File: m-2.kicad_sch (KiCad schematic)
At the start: 26 parts, among them J2 1-2199230-6, Y1 ECS-327MVATX-2-CN-TR3

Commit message: Layout cleanup, silk
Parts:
- TP10, TP11, TP12: footprint JetsonCarrier:TP_SMD_0.75mm -> TestPoint:TestPoint_Pad_D1.0mm
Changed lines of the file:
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@@
 			)
 		)
-		(property "Footprint" "JetsonCarrier:TP_SMD_0.75mm"
+		(property "Footprint" "TestPoint:TestPoint_Pad_D1.0mm"
 			(at 245.11 128.27 0)
 			(hide yes)
@@
 			)
 		)
-		(property "Footprint" "JetsonCarrier:TP_SMD_0.75mm"
+		(property "Footprint" "TestPoint:TestPoint_Pad_D1.0mm"
 			(at 245.11 130.81 0)
 			(hide yes)
@@
 			)
 		)
-		(property "Footprint" "JetsonCarrier:TP_SMD_0.75mm"
+		(property "Footprint" "TestPoint:TestPoint_Pad_D1.0mm"
 			(at 245.11 133.35 0)
 			(hide yes)

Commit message: route all diff pairs, length tuning
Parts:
- renumbered C25 to C10, C13 to C11, C14 to C12, C15 to C13, C16 to C14, C17 to C15, C18 to C16, C19 to C17, C20 to C18, C21 to C19, C22 to C20, C23 to C21, C24 to C22, D1 to D3, R13 to R16, R37 to R17, R38 to R18, R39 to R19, R19 to R20, R143 to R21, TP10 to TP3, TP11 to TP4, TP12 to TP5

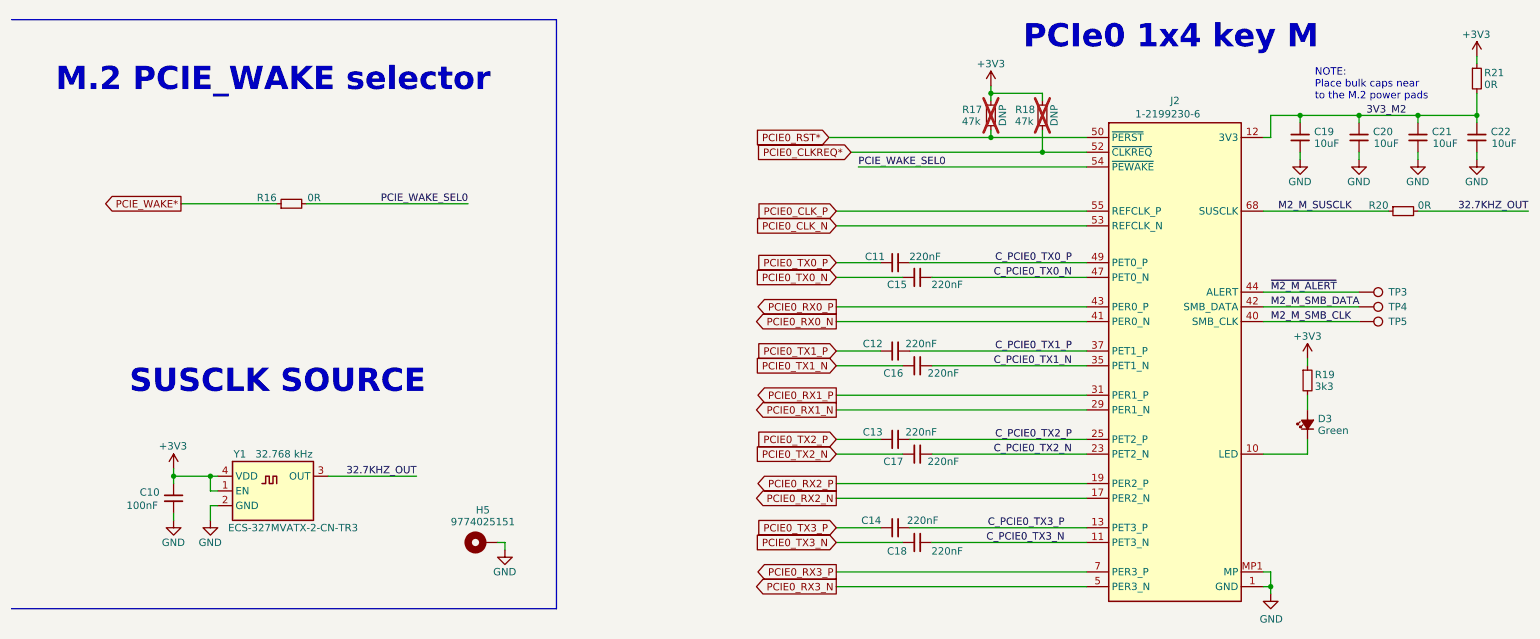
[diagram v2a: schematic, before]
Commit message: Replace current monitor w/ INA226 (addr = 0x42)
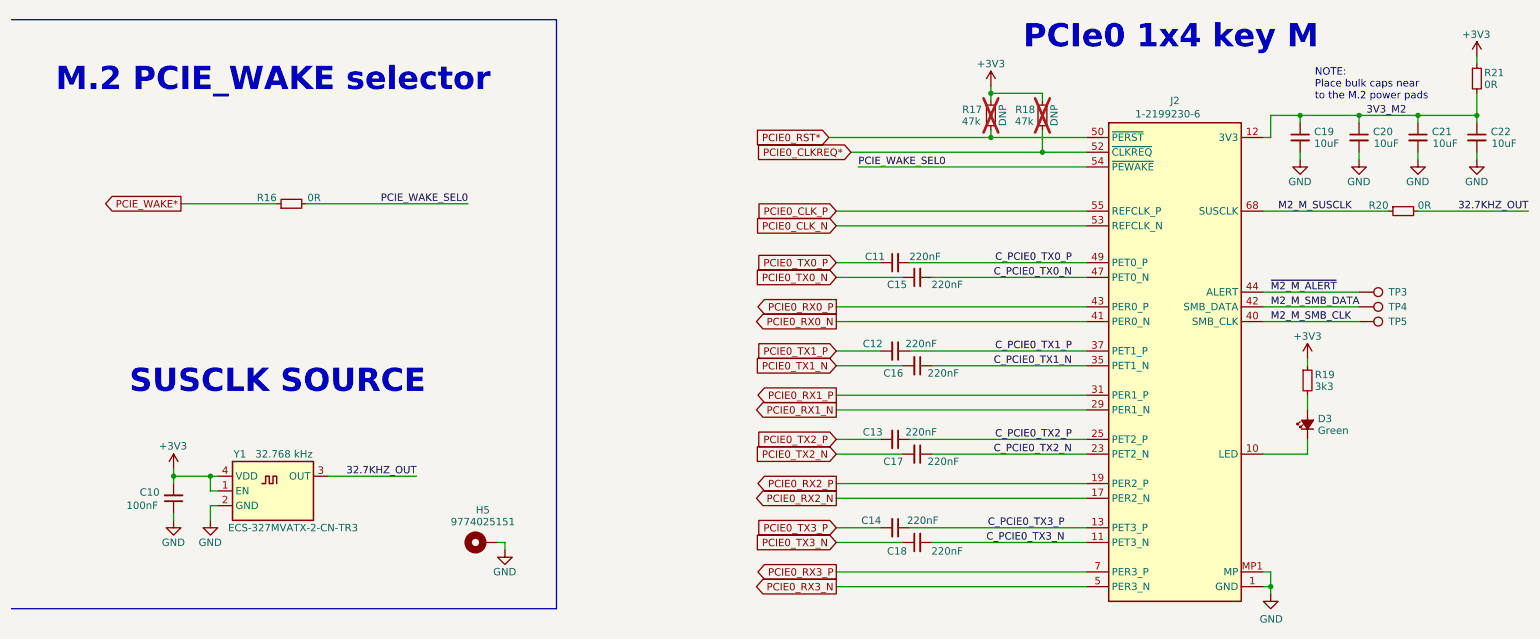
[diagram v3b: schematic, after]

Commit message: Final BOM changes, gerbers
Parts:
- C10: LCSC (none) -> C14663
- C11, C12, C13, C14, C15, C16, C17, C18: LCSC (none) -> C16772
- C19, C20, C21, C22: LCSC (none) -> C96446
- D3: LCSC (none) -> C12065
- J2: LCSC (none) -> C4710843
- R16, R20: LCSC (none) -> C17168
- R17, R18: LCSC (none) -> C25792
- R19: LCSC (none) -> C22978
- R21: LCSC (none) -> C21189
- Y1: LCSC (none) -> C5375606
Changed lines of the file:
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@@
 			)
 		)
+		(property "LCSC" "C5375606"
+			(at 52.07 151.13 0)
+			(effects
+				(font
+					(size 1.27 1.27)
+				)
+				(hide yes)
+			)
+		)
 		(pin "2"
 		)
@@
 			)
 		)
+		(property "LCSC" "C25792"
+			(at 189.23 92.456 0)
+			(effects
+				(font
+					(size 1.27 1.27)
+				)
+				(hide yes)
+			)
+		)
 		(pin "1"
 		)
@@
 			)
 		)
+		(property "LCSC" "C16772"
+			(at 159.512 132.842 0)
+			(effects
+				(font
+					(size 1.27 1.27)
+				)
+				(hide yes)
+			)
+		)
 		(pin "1"
 		)
@@
 			)
 		)
+		(property "LCSC" "C14663"
+			(at 34.798 156.972 0)
+			(effects
+				(font
+					(size 1.27 1.27)
+				)
+				(hide yes)
+			)
+		)
 		(pin "1"
 		)
@@
 			)
 		)
+		(property "LCSC" "C16772"
+			(at 167.132 121.158 0)
+			(effects
+				(font
+					(size 1.27 1.27)
+				)
+				(hide yes)
+			)
+		)
 		(pin "1"
 		)
@@
 			)
 		)
+		(property "LCSC" "C12065"
+			(at 237.998 145.034 0)
+			(effects
+				(font
+					(size 1.27 1.27)
+				)
+				(hide yes)
+			)
+		)
 		(pin "1"
 		)
@@
 			)
 		)
+		(property "LCSC" "C16772"
+			(at 159.512 148.082 0)
+			(effects
+				(font
+					(size 1.27 1.27)
+				)
+				(hide yes)
+			)
+		)
 		(pin "1"
 		)
@@
 			)
 		)
+		(property "LCSC" "C22978"
+			(at 237.49 138.176 0)
+			(effects
+				(font
+					(size 1.27 1.27)
+				)
+				(hide yes)
+			)
+		)
 		(pin "1"
 		)
@@
 			)
 		)
+		(property "LCSC" "C96446"
+			(at 261.112 96.266 0)
+			(effects
+				(font
+					(size 1.27 1.27)
+				)
+				(hide yes)
+			)
+		)
 		(pin "1"
 		)
@@
 			)
 		)
+		(property "LCSC" "C16772"
+			(at 163.068 137.922 0)
+			(effects
+				(font
+					(size 1.27 1.27)
+				)
+				(hide yes)
+			)
+		)
 		(pin "1"
 		)
@@
 			)
 		)
+		(property "LCSC" "C25792"
+			(at 180.086 92.456 0)
+			(effects
+				(font
+					(size 1.27 1.27)
+				)
+				(hide yes)
+			)
+		)
 		(pin "1"
 		)
@@
 			)
 		)
+		(property "LCSC" "C96446"
+			(at 250.952 96.266 0)
+			(effects
+				(font
+					(size 1.27 1.27)
+				)
+				(hide yes)
+			)
+		)
 		(pin "1"
 		)
@@
 			)
 		)
+		(property "LCSC" "C96446"
+			(at 271.272 96.266 0)
+			(effects
+				(font
+					(size 1.27 1.27)
+				)
+				(hide yes)
+			)
+		)
 		(pin "1"
 		)
@@
 			)
 		)
+		(property "LCSC" "C96446"
+			(at 240.792 96.266 0)
+			(effects
+				(font
+					(size 1.27 1.27)
+				)
+				(hide yes)
+			)
+		)
 		(pin "1"
 		)
@@
 			)
 		)
+		(property "LCSC" "C21189"
+			(at 266.7 86.106 0)
+			(effects
+				(font
+					(size 1.27 1.27)
+				)
+				(hide yes)
+			)
+		)
 		(pin "1"
 		)
@@
 			)
 		)
+		(property "LCSC" "C4710843"
+			(at 213.36 90.17 0)
+			(effects
+				(font
+					(size 1.27 1.27)
+				)
+				(hide yes)
+			)
+		)
 		(pin "1"
 		)
@@
 			)
 		)
+		(property "LCSC" "C17168"
+			(at 250.19 108.966 0)
+			(effects
+				(font
+					(size 1.27 1.27)
+				)
+				(hide yes)
+			)
+		)
 		(pin "1"
 		)
@@
 			)
 		)
+		(property "LCSC" "C16772"
+			(at 163.068 153.162 0)
+			(effects
+				(font
+					(size 1.27 1.27)
+				)
+				(hide yes)
+			)
+		)
 		(pin "1"
 		)
@@
 			)
 		)
+		(property "LCSC" "C17168"
+			(at 58.42 106.172 0)
+			(effects
+				(font
+					(size 1.27 1.27)
+				)
+				(hide yes)
+			)
+		)
 		(pin "1"
 		)
@@
 			)
 		)
+		(property "LCSC" "C16772"
+			(at 167.132 167.132 0)
+			(effects
+				(font
+					(size 1.27 1.27)
+				)
+				(hide yes)
+			)
+		)
 		(pin "1"
 		)
@@
 			)
 		)
+		(property "LCSC" "C16772"
+			(at 159.258 163.322 0)
+			(effects
+				(font
+					(size 1.27 1.27)
+				)
+				(hide yes)
+			)
+		)
 		(pin "1"
 		)
@@
 			)
 		)
+		(property "LCSC" "C16772"
+			(at 163.322 116.332 0)
+			(effects
+				(font
+					(size 1.27 1.27)
+				)
+				(hide yes)
+			)
+		)
